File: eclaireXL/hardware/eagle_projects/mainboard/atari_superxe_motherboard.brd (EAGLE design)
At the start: 140.6 x 100.1 mm, 121 parts

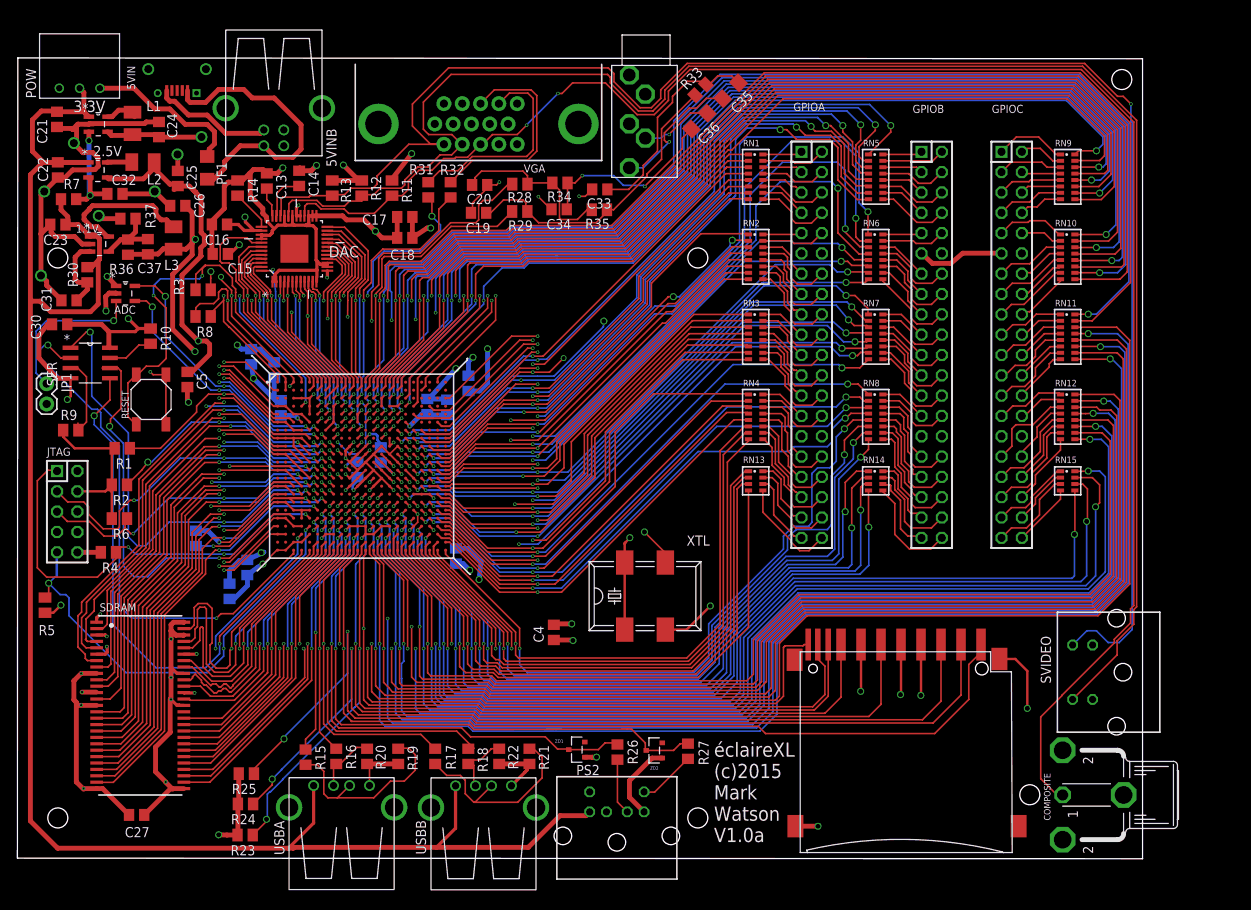
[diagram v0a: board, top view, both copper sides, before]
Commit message: Fixed audio connector footprint/location. Fixed oscilator footprint (fitted but was too large). Added 16 pin support for serial init rom. Moved reset switch location to allow this. Added pull ups and decoupling to ADC (still untested). Added some more 2.5mm drill holes on the right for stencil positioning. Increased 2.5mm drill size by 1 notch (was too small to fit). Added solder pads for din connectors. Fixed footprint for phono connector. Increased resistor array size to allow fixing by hand more easily. Added pin headers to allow bypassing resistor arrays in case of issues soldering thsm! Added pin header borders to board to make it clear how much space is needed around them for sockets. Made room for jtag pin header socket. Increased version to v1.1. Added decoupling cap to oscillator. Added voltage test point header. Power ADC by 5V (it allows 2.7V to 5.5v but higher reduces changes of breaking it by high voltage inputs I think). Think thats it. Will review a bit then make the next board revision.
git-svn-id: http://www.64kib.com/atarixlfpga_svn/trunk/atari_800xl@408 d6161ac3-aae1-4d52-9b05-ea9ac36b53d3
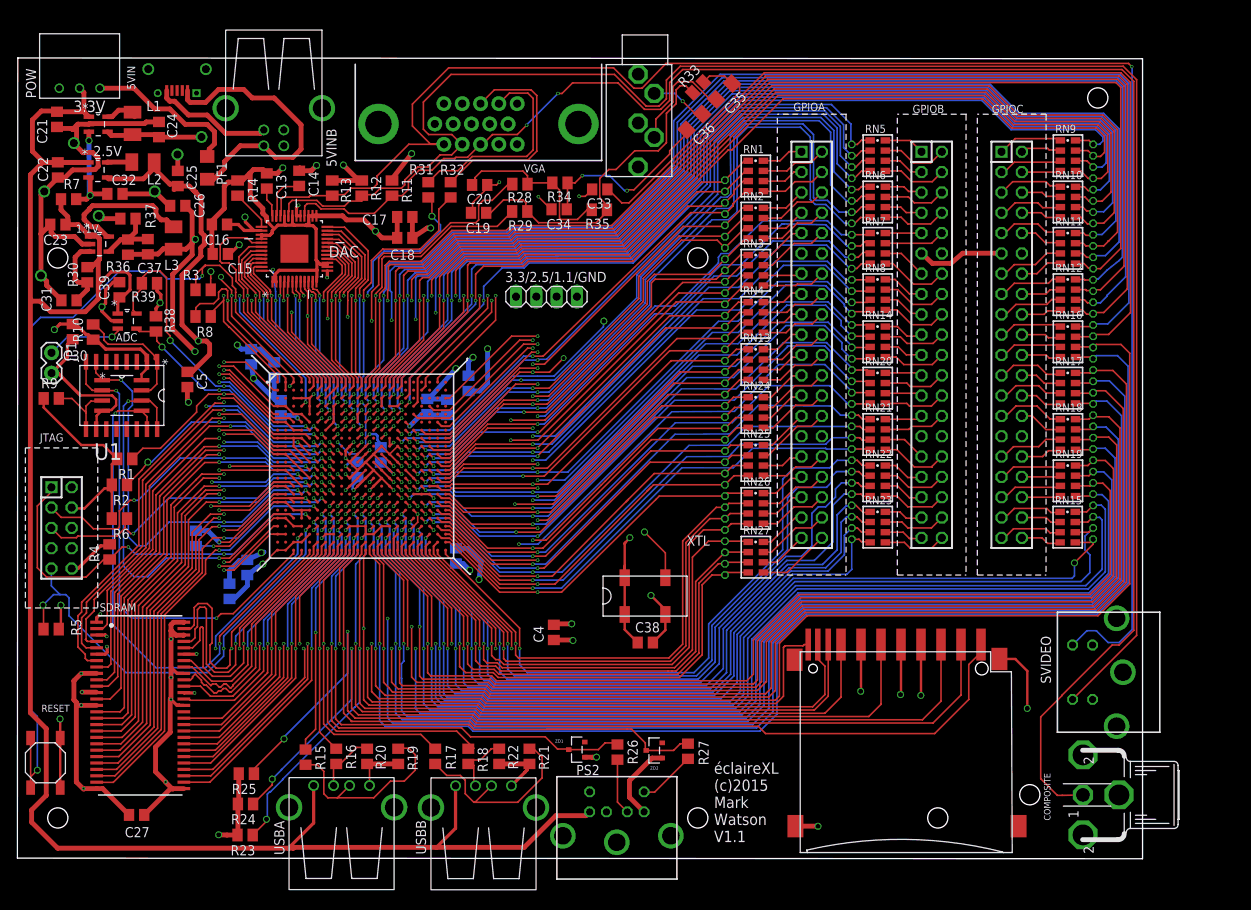
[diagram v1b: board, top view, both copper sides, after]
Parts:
- removed SER: AT25320B-SSHL-B, Atmel_By_element14_Batch_1-00:SOIC127P600X175-8N
- added 3.3/2.5/1.1/GND: (no value), pinhead:1X04
- added C38, C39: 0.1uF, rcl:C0805
- added R38, R39: 2k, rcl:M0805
- added RN16, RN17, RN18, RN19, RN20, RN21, RN22, RN23, RN24, RN25, RN26, RN27: 47, resistor-array:743-8
- added U$3, U$4, U$5: HDR_SMALL_36_DEV_LALIGNED, header127:HDR_141_36
- added U1: EPCS, epcs:EPCS_BOTH
- COMPOSITE: value TOBU3 -> TOBU3MINE; device con-hirschmann:TOBU3 -> con-hirschmann:TOBU3_EXT
- JTAG: value M-2X05-DIL-100 -> M-2X05-BORDER; device con-headers-jp:DIL-100-2X05 -> con-headers-jp:DIL-100-2X05-BRD
- RN1, RN10, RN11, RN12, RN2, RN3, RN4, RN5, RN6, RN7, RN8, RN9: device resistor-array:742-16 -> resistor-array:743-8
- RN13, RN14, RN15: device resistor-array:742-8 -> resistor-array:743-8
- XTL: device crystal:1100S -> crystal:SG-636
- moved RESET 47.3 mm to (3.45, 11.9)
- moved RN14 17.4 mm to (107.5, 64.5)
- moved RN8 15.3 mm to (107.5, 70.4)
- moved RN12 15.3 mm to (131.3, 70.4)
- moved RN13 14.5 mm to (92.3, 61.7)
- moved RN4 12.4 mm to (92.3, 67.6)
- moved RN7 11.1 mm to (107.5, 76.2)
- moved RN11 11.1 mm to (131.3, 76.2)
- moved RN3 8.32 mm to (92.3, 73.5)
- moved R10 7.19 mm to (9.42, 65.7), turned to 90 degrees
- moved RN6 6.86 mm to (107.5, 82.0)
- moved RN10 6.85 mm to (131.3, 82.0)
- moved RN15 5.79 mm to (131.2, 41.3)
- moved R9 4.65 mm to (4.18, 57.4)
- moved RN2 4.21 mm to (92.3, 79.3)
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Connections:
- net 1V1: now also 3.3/2.5/1.1/GND.3
- net 2V5: now also 3.3/2.5/1.1/GND.2
- net 3V3: now also 3.3/2.5/1.1/GND.1, C38.1, R38.2, R39.1, U1.8, U1.L$2, XTL.P$1, XTL.P$4; no longer ADC.1, SER.8, XTL.1, XTL.4
- net 5V0: now also ADC.1, C39.1
- net GND: now also 3.3/2.5/1.1/GND.4, C38.2, C39.2, U1.4, U1.L$10, XTL.P$2; no longer SER.4, XTL.2
- net GPIOA0: now also U$5.P$1
- net GPIOA1: now also U$5.P$2
- net GPIOA10: now also RN3.3, U$5.P$11; no longer RN2.3
- net GPIOA11: now also RN3.4, U$5.P$12; no longer RN2.4
- net GPIOA12: now also RN4.1, U$5.P$13; no longer RN2.5
- net GPIOA13: now also RN4.2, U$5.P$14; no longer RN2.6
- net GPIOA14: now also RN4.3, U$5.P$15; no longer RN2.7
- net GPIOA15: now also RN4.4, U$5.P$16; no longer RN2.8
- net GPIOA16: now also RN13.1, U$5.P$17; no longer RN3.1
- net GPIOA17: now also RN13.2, U$5.P$18; no longer RN3.2
- net GPIOA18: now also RN13.3, U$5.P$19; no longer RN3.3
- net GPIOA19: now also RN13.4, U$5.P$20; no longer RN3.4
- net GPIOA2: now also U$5.P$3
- net GPIOA20: now also RN24.1, U$5.P$21; no longer RN3.5
- net GPIOA21: now also RN24.2, U$5.P$22; no longer RN3.6
- net GPIOA22: now also RN24.3, U$5.P$23; no longer RN3.7
- net GPIOA23: now also RN24.4, U$5.P$24; no longer RN3.8
- net GPIOA24: now also RN25.1, U$5.P$25; no longer RN4.1
- net GPIOA25: now also RN25.2, U$5.P$26; no longer RN4.2
- net GPIOA26: now also RN25.3, U$5.P$27; no longer RN4.3
- net GPIOA27: now also RN25.4, U$5.P$28; no longer RN4.4
- net GPIOA28: now also RN26.1, U$5.P$29; no longer RN4.5
- net GPIOA29: now also RN26.2, U$5.P$30; no longer RN4.6
- net GPIOA3: now also U$5.P$4
- net GPIOA30: now also RN26.3, U$5.P$31; no longer RN4.7
- net GPIOA31: now also RN26.4, U$5.P$32; no longer RN4.8
- net GPIOA32: now also RN27.1, U$5.P$33; no longer RN13.1
- net GPIOA33: now also RN27.2, U$5.P$34; no longer RN13.2
- net GPIOA34: now also RN27.3, U$5.P$35; no longer RN13.3
- net GPIOA35: now also RN27.4, U$5.P$36; no longer RN13.4
- net GPIOA4: now also RN2.1, U$5.P$5; no longer RN1.5
- net GPIOA5: now also RN2.2, U$5.P$6; no longer RN1.6
- net GPIOA6: now also RN2.3, U$5.P$7; no longer RN1.7
- net GPIOA7: now also RN2.4, U$5.P$8; no longer RN1.8
- net GPIOA8: now also RN3.1, U$5.P$9; no longer RN2.1
- net GPIOA9: now also RN3.2, U$5.P$10; no longer RN2.2
- net GPIOB0: now also U$4.P$1
- net GPIOB1: now also U$4.P$2
- net GPIOB10: now also RN7.3, U$4.P$11; no longer RN6.3
- net GPIOB11: now also RN7.4, U$4.P$12; no longer RN6.4
- net GPIOB12: now also RN8.1, U$4.P$13; no longer RN6.5
- net GPIOB13: now also RN8.2, U$4.P$14; no longer RN6.6
- net GPIOB14: now also RN8.3, U$4.P$15; no longer RN6.7
- net GPIOB15: now also RN8.4, U$4.P$16; no longer RN6.8
- net GPIOB16: now also RN14.1, U$4.P$17; no longer RN7.1
- net GPIOB17: now also RN14.2, U$4.P$18; no longer RN7.2
- net GPIOB18: now also RN14.3, U$4.P$19; no longer RN7.3
- net GPIOB19: now also RN14.4, U$4.P$20; no longer RN7.4
- net GPIOB2: now also U$4.P$3
- net GPIOB20: now also RN20.1, U$4.P$21; no longer RN7.5
- net GPIOB21: now also RN20.2, U$4.P$22; no longer RN7.6
- net GPIOB22: now also RN20.3, U$4.P$23; no longer RN7.7
- net GPIOB23: now also RN20.4, U$4.P$24; no longer RN7.8
- net GPIOB24: now also RN21.1, U$4.P$25; no longer RN8.1
- net GPIOB25: now also RN21.2, U$4.P$26; no longer RN8.2
- net GPIOB26: now also RN21.3, U$4.P$27; no longer RN8.3
- net GPIOB27: now also RN21.4, U$4.P$28; no longer RN8.4
- net GPIOB28: now also RN22.1, U$4.P$29; no longer RN8.5
- net GPIOB29: now also RN22.2, U$4.P$30; no longer RN8.6
- net GPIOB3: now also U$4.P$4
- net GPIOB30: now also RN22.3, U$4.P$31; no longer RN8.7
- net GPIOB31: now also RN22.4, U$4.P$32; no longer RN8.8
- net GPIOB32: now also RN23.1, U$4.P$33; no longer RN14.1
- net GPIOB33: now also RN23.2, U$4.P$34; no longer RN14.2
- net GPIOB34: now also RN23.3, U$4.P$35; no longer RN14.3
- net GPIOB35: now also RN23.4, U$4.P$36; no longer RN14.4
- net GPIOB4: now also RN6.1, U$4.P$5; no longer RN5.5
- net GPIOB5: now also RN6.2, U$4.P$6; no longer RN5.6
- net GPIOB6: now also RN6.3, U$4.P$7; no longer RN5.7
- net GPIOB7: now also RN6.4, U$4.P$8; no longer RN5.8
- net GPIOB8: now also RN7.1, U$4.P$9; no longer RN6.1
- net GPIOB9: now also RN7.2, U$4.P$10; no longer RN6.2
- net GPIOC0: now also RN9.8, U$3.P$1; no longer RN9.16
- net GPIOC1: now also RN9.7, U$3.P$2; no longer RN9.15
- net GPIOC10: now also RN11.6, U$3.P$11; no longer RN10.14
- net GPIOC11: now also RN11.5, U$3.P$12; no longer RN10.13
- net GPIOC12: now also RN12.8, U$3.P$13; no longer RN10.12
- net GPIOC13: now also RN12.7, U$3.P$14; no longer RN10.11
- net GPIOC14: now also RN12.6, U$3.P$15; no longer RN10.10
- net GPIOC15: now also RN12.5, U$3.P$16; no longer RN10.9
- net GPIOC16: now also RN16.8, U$3.P$17; no longer RN11.16
- net GPIOC17: now also RN16.7, U$3.P$18; no longer RN11.15
- net GPIOC18: now also RN16.6, U$3.P$19; no longer RN11.14
- net GPIOC19: now also RN16.5, U$3.P$20; no longer RN11.13
- net GPIOC2: now also RN9.6, U$3.P$3; no longer RN9.14
- net GPIOC20: now also RN17.8, U$3.P$21; no longer RN11.12
- net GPIOC21: now also RN17.7, U$3.P$22; no longer RN11.11
- net GPIOC22: now also RN17.6, U$3.P$23; no longer RN11.10
- net GPIOC23: now also RN17.5, U$3.P$24; no longer RN11.9
- net GPIOC24: now also RN18.8, U$3.P$25; no longer RN12.16
- net GPIOC25: now also RN18.7, U$3.P$26; no longer RN12.15
- net GPIOC26: now also RN18.6, U$3.P$27; no longer RN12.14
- net GPIOC27: now also RN18.5, U$3.P$28; no longer RN12.13
- net GPIOC28: now also RN19.8, U$3.P$29; no longer RN12.12
- net GPIOC29: now also RN19.7, U$3.P$30; no longer RN12.11
- net GPIOC3: now also RN9.5, U$3.P$4; no longer RN9.13
- net GPIOC30: now also RN19.6, U$3.P$31; no longer RN12.10
- net GPIOC31: now also RN19.5, U$3.P$32; no longer RN12.9
- net GPIOC32: now also U$3.P$33
- net GPIOC33: now also U$3.P$34
- net GPIOC34: now also U$3.P$35
- net GPIOC35: now also U$3.P$36
- net GPIOC4: now also RN10.8, U$3.P$5; no longer RN9.12
- net GPIOC5: now also RN10.7, U$3.P$6; no longer RN9.11
- net GPIOC6: now also RN10.6, U$3.P$7; no longer RN9.10
- net GPIOC7: now also RN10.5, U$3.P$8; no longer RN9.9
- net GPIOC8: now also RN11.8, U$3.P$9; no longer RN10.16
- net GPIOC9: now also RN11.7, U$3.P$10; no longer RN10.15
- net N$10: now also U1.3, U1.L$9; no longer SER.3
- net N$103: now also RN10.1; no longer RN9.5
- net N$104: now also RN10.2; no longer RN9.6
- net N$105: now also RN10.3; no longer RN9.7
- net N$106: now also RN10.4; no longer RN9.8
- net N$107: now also RN11.1; no longer RN10.1
- net N$108: now also RN11.2; no longer RN10.2
- net N$109: now also RN11.3; no longer RN10.3
- net N$11: now also U1.7, U1.L$1; no longer SER.7
- net N$110: now also RN11.4; no longer RN10.4
- net N$111: now also RN12.1; no longer RN10.5
- net N$112: now also RN12.2; no longer RN10.6
- net N$113: now also RN12.3; no longer RN10.7
- net N$114: now also RN12.4; no longer RN10.8
- net N$115: now also RN16.1; no longer RN11.1
- net N$116: now also RN16.2; no longer RN11.2
- net N$117: now also RN16.3; no longer RN11.3
- net N$118: now also RN16.4; no longer RN11.4
- net N$119: now also RN17.1; no longer RN11.5
- net N$12: now also XTL.P$3; no longer XTL.3
- net N$120: now also RN17.2; no longer RN11.6
- net N$121: now also RN17.3; no longer RN11.7
- net N$122: now also RN17.4; no longer RN11.8
- net N$123: now also RN18.1; no longer RN12.1
- net N$124: now also RN18.2; no longer RN12.2
- net N$125: now also RN18.3; no longer RN12.3
- net N$126: now also RN18.4; no longer RN12.4
- net N$127: now also RN19.1; no longer RN12.5
- net N$128: now also RN19.2; no longer RN12.6
- net N$129: now also RN19.3; no longer RN12.7
- net N$130: now also RN19.4; no longer RN12.8
- net N$138: now also AUDIO.P$3; no longer AUDIO.P$5
- net N$141: now also AUDIO.P$2; no longer AUDIO.P$4
- net N$22: now also RN1.8; no longer RN1.16
- net N$24: now also RN1.7; no longer RN1.15
- net N$29: now also RN1.6; no longer RN1.14
- net N$30: now also RN1.5; no longer RN1.13
- net N$31: now also RN2.8; no longer RN1.12
- net N$32: now also RN2.7; no longer RN1.11
- net N$33: now also RN2.6; no longer RN1.10
- net N$34: now also RN2.5; no longer RN1.9
- net N$35: now also RN3.8; no longer RN2.16
- net N$36: now also RN3.7; no longer RN2.15
- net N$37: now also RN3.6; no longer RN2.14
- net N$38: now also RN3.5; no longer RN2.13
- net N$39: now also RN4.8; no longer RN2.12
- net N$40: now also RN4.6; no longer RN2.10
- net N$41: now also RN4.7; no longer RN2.11
- net N$42: now also RN4.5; no longer RN2.9
- net N$43: now also RN13.8; no longer RN3.16
- net N$44: now also RN13.7; no longer RN3.15
- net N$45: now also RN13.6; no longer RN3.14
- net N$46: now also RN13.5; no longer RN3.13
- net N$47: now also RN24.8; no longer RN3.12
- net N$48: now also RN24.6; no longer RN3.10
- net N$49: now also RN24.7; no longer RN3.11
- net N$50: now also RN24.5; no longer RN3.9
- net N$51: now also RN25.8; no longer RN4.16
- net N$52: now also RN25.7; no longer RN4.15
- net N$53: now also RN25.6; no longer RN4.14
- net N$54: now also RN25.5; no longer RN4.13
- net N$55: now also RN26.8; no longer RN4.12
- net N$56: now also RN26.7; no longer RN4.11
- net N$57: now also RN26.6; no longer RN4.10
- net N$58: now also RN26.5; no longer RN4.9
- net N$59: now also RN27.8; no longer RN13.8
- net N$6: now also U1.6, U1.L$16; no longer SER.6
- net N$60: now also RN27.7; no longer RN13.7
- net N$61: now also RN27.6; no longer RN13.6
- net N$62: now also RN27.5; no longer RN13.5
- net N$63: now also RN5.8; no longer RN5.16
- net N$64: now also RN5.7; no longer RN5.15
- net N$65: now also RN5.6; no longer RN5.14
- net N$66: now also RN5.5; no longer RN5.13
- net N$67: now also RN6.8; no longer RN5.12
- net N$68: now also RN6.7; no longer RN5.11
- net N$69: now also RN6.6; no longer RN5.10
- net N$7: now also U1.1, U1.L$7; no longer SER.1
- net N$70: now also RN6.5; no longer RN5.9
- net N$71: now also RN7.8; no longer RN6.16
- net N$72: now also RN7.7; no longer RN6.15
- net N$73: now also RN7.6; no longer RN6.14
- net N$74: now also RN7.5; no longer RN6.13
- net N$75: now also RN8.8; no longer RN6.12
- net N$76: now also RN8.7; no longer RN6.11
- net N$77: now also RN8.6; no longer RN6.10
- net N$78: now also RN8.5; no longer RN6.9
- net N$79: now also RN14.8; no longer RN7.16
- net N$8: now also U1.2, U1.L$8; no longer SER.2
- net N$80: now also RN14.7; no longer RN7.15
- net N$81: now also RN14.6; no longer RN7.14
- net N$82: now also RN14.5; no longer RN7.13
- net N$83: now also RN20.8; no longer RN7.12
- net N$84: now also RN20.7; no longer RN7.11
- net N$85: now also RN20.6; no longer RN7.10
- net N$86: now also RN20.5; no longer RN7.9
- net N$87: now also RN21.8; no longer RN8.16
- net N$88: now also RN21.7; no longer RN8.15
- net N$89: now also RN21.6; no longer RN8.14
- net N$9: now also U1.5, U1.L$15; no longer SER.5
- net N$90: now also RN21.5; no longer RN8.13
- net N$91: now also RN22.8; no longer RN8.12
- net N$92: now also RN22.7; no longer RN8.11
- net N$93: now also RN22.6; no longer RN8.10
- net N$94: now also RN22.5; no longer RN8.9
- net N$95: now also RN23.8; no longer RN14.8
- net N$96: now also RN23.7; no longer RN14.7
- net N$97: now also RN23.6; no longer RN14.6
- net N$98: now also RN23.5; no longer RN14.5
- net SCL: now also R39.2
- net SDA: now also R38.1
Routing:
- net CONFIG_N: track 53.8 -> 113.7 mm
- net 5V0: track 361.2 -> 409.5 mm
- net GPIOB8: track 92.4 -> 72.1 mm, vias 3 -> 2
- net GPIOB9: track 84.5 -> 66.8 mm, vias 2 -> 1
- net GPIOB10: track 85.4 -> 70.4 mm, vias 3 -> 2
- net GPIOB11: track 77.3 -> 66.2 mm, vias 2 -> 1
- net 3V3: track 479.6 -> 490.5 mm
- net AUDIO_IN: track 19.9 -> 9.73 mm
- net N$11: track 5.81 -> 15.7 mm
- net GPIOA34: track 73.5 -> 64.0 mm
- net GPIOA33: track 73.6 -> 64.3 mm
- net GPIOA30: track 73.9 -> 64.7 mm
- net GPIOA29: track 71.1 -> 61.9 mm
- net GPIOA35: track 79.1 -> 70.0 mm
- net GND: track 840.9 -> 850.0 mm, vias 92 -> 91
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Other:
- board text added: "éclaireXL (c)2015 Mark Watson V1.1"
- board text removed: "éclaireXL (c)2015 Mark Watson V1.0a"

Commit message: Moved traces away from mounting holes to remove risk of taking out traces with screws... Harder than expected!
git-svn-id: http://www.64kib.com/atarixlfpga_svn/trunk/atari_800xl@409 d6161ac3-aae1-4d52-9b05-ea9ac36b53d3
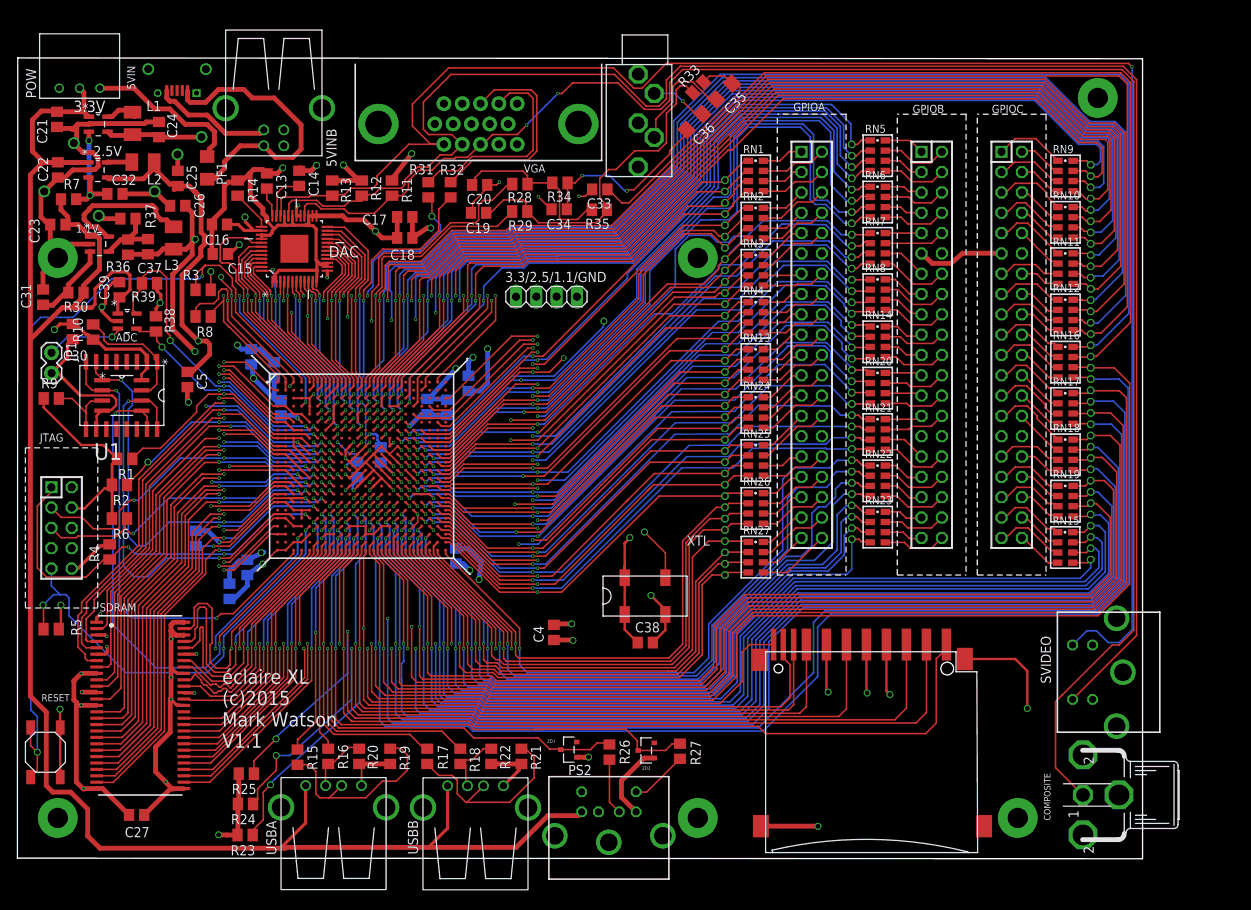
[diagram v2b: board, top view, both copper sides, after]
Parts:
- added H1, H2, H3, H4, H5, H6: MOUNT-PAD-ROUND2.5, holes:2,5-PAD
- moved U$2 4.32 mm to (106.7, 25.8)
- moved C31 3.28 mm to (3.15, 70.1), turned to 90 degrees
- moved R30 2.65 mm to (7.26, 70.7), turned to 180 degrees
- moved RN10 2.56 mm to (131.0, 79.5)
- moved RN11 2.56 mm to (131.0, 73.7)
- moved RN12 2.56 mm to (131.0, 67.9)
- moved RN16 2.56 mm to (131.0, 62.0)
- moved RN15 2.56 mm to (130.9, 38.8)
- moved RN17 2.56 mm to (131.0, 56.2)
- moved RN18 2.56 mm to (131.0, 50.4)
- moved RN19 2.56 mm to (131.0, 44.6)
- moved U$3 2.56 mm to (134.1, 61.3)
- moved RN9 2.56 mm to (131.0, 85.2)
- moved RESET 1.32 mm to (3.45, 13.2)
- moved PS2 1.00 mm to (73.9, -2.74)
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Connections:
- net GND: now also H1.B2,8, H2.B2,8, H3.B2,8, H4.B2,8, H5.B2,8, H6.B2,8
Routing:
- net GPIOB8: track 72.1 -> 78.2 mm
- net SD_WRITEPROTECT: track 85.0 -> 79.3 mm
- net GND: track 850.0 -> 855.5 mm, vias 91 -> 90
- net GPIOC19: track 164.5 -> 160.2 mm
- net SD_DETECT: track 90.0 -> 85.9 mm
- net SD_SCK: track 99.6 -> 95.7 mm
- net GPIOC18: track 162.6 -> 158.7 mm
- net SD_MOSI: track 135.0 -> 131.1 mm
- net SD_DAT1: track 84.6 -> 80.9 mm
- net CONFIG_N: track 113.7 -> 110.2 mm
- net SD_MISO: track 117.5 -> 114.1 mm
- net N$143: track 217.2 -> 213.8 mm
- net GPIOC21: track 164.3 -> 160.9 mm
- net 3V3: track 490.5 -> 493.4 mm
- net GPIOC25: track 148.5 -> 145.7 mm
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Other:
- board text added: "éclaire XL (c)2015 Mark Watson V1.1"
- board text removed: "éclaireXL (c)2015 Mark Watson V1.1"

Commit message: DE1 connector spacing (20mm). Improved mounting holes.
git-svn-id: http://www.64kib.com/atarixlfpga_svn/trunk/atari_800xl@411 d6161ac3-aae1-4d52-9b05-ea9ac36b53d3
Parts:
- moved H6 20.0 mm to (145.0, 5.00)
- moved GPIOC 15.0 mm to (139.2, 64.1)
- moved R25 10.3 mm to (20.0, 4.79), turned to 270 degrees
- moved H1 10.0 mm to (145.0, 95.0)
- moved SVIDEO 9.79 mm to (152.1, 20.1)
- moved U$3 5.51 mm to (129.0, 59.2)
- moved R24 5.07 mm to (23.8, 4.69), turned to 270 degrees
- moved GPIOB 5.00 mm to (119.2, 64.1)
- moved RN14 5.00 mm to (112.5, 64.5)
- moved RN20 5.00 mm to (112.5, 58.7)
- moved RN21 5.00 mm to (112.5, 52.9)
- moved RN22 5.00 mm to (112.5, 47.1)
- moved RN23 5.00 mm to (112.5, 41.4)
- moved RN5 5.00 mm to (112.5, 87.8)
- moved RN6 5.00 mm to (112.5, 82.0)
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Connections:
- removed net N$134: GPIOC.40, RN15.4
- new net N$15: GPIOC.1, RN9.8
- net GPIOC0: now also RN9.1, U$1.B12; no longer RN9.8, U$1.C15
- net GPIOC1: now also RN9.2, U$1.D12; no longer RN9.7, U$1.E15
- net GPIOC10: now also RN11.3, U$1.A14; no longer RN11.6, U$1.C13
- net GPIOC11: now also RN11.4, U$1.E14; no longer RN11.5, U$1.D13
- net GPIOC12: now also RN12.1, U$1.F14; no longer RN12.8, U$1.B13
- net GPIOC13: now also RN12.2, U$1.H14; no longer RN12.7, U$1.A13
- net GPIOC14: now also RN12.3, U$1.A15; no longer RN12.6, U$1.F12
- net GPIOC15: now also RN12.4, U$1.B15; no longer RN12.5, U$1.E12
- net GPIOC16: now also RN16.1, U$1.E15; no longer RN16.8, U$1.D12
- net GPIOC17: now also RN16.2, U$1.C15; no longer RN16.7, U$1.B12
- net GPIOC18: now also RN16.3, U$1.Y16; no longer RN16.6, U$1.V13
- net GPIOC19: now also RN16.4, U$1.V16; no longer RN16.5, U$1.AA13
- net GPIOC2: now also RN9.3, U$1.E12; no longer RN9.6, U$1.B15
- net GPIOC20: now also RN17.1, U$1.W16; no longer RN17.8, U$1.AB13
- net GPIOC21: now also RN17.2, U$1.U16; no longer RN17.7, U$1.R14
- net GPIOC22: now also RN17.3, U$1.AB15; no longer RN17.6, U$1.T14
- net GPIOC23: now also RN17.4, U$1.AA15; no longer RN17.5, U$1.Y14
- net GPIOC24: now also RN18.1, U$1.V15; no longer RN18.8, U$1.V14
- net GPIOC25: now also RN18.2, U$1.Y15; no longer RN18.7, U$1.AA14
- net GPIOC26: now also RN18.3, U$1.U15; no longer RN18.6, U$1.T15
- net GPIOC27: now also RN18.4, U$1.T15; no longer RN18.5, U$1.U15
- net GPIOC28: now also RN19.1, U$1.AA14; no longer RN19.8, U$1.Y15
- net GPIOC29: now also RN19.2, U$1.V14; no longer RN19.7, U$1.V15
- net GPIOC3: now also RN9.4, U$1.F12; no longer RN9.5, U$1.A15
- net GPIOC30: now also RN19.3, U$1.Y14; no longer RN19.6, U$1.AA15
- net GPIOC31: now also RN19.4, U$1.T14; no longer RN19.5, U$1.AB15
- net GPIOC32: now also RN15.1, U$1.R14; no longer RN15.8, U$1.U16
- net GPIOC33: now also RN15.2, U$1.AB13; no longer RN15.7, U$1.W16
- net GPIOC34: now also RN15.3, U$1.AA13; no longer RN15.6, U$1.V16
- net GPIOC35: now also RN15.4, U$1.V13; no longer RN15.5, U$1.Y16
- net GPIOC4: now also RN10.1, U$1.A13; no longer RN10.8, U$1.H14
- net GPIOC5: now also RN10.2, U$1.B13; no longer RN10.7, U$1.F14
- net GPIOC6: now also RN10.3, U$1.D13; no longer RN10.6, U$1.E14
- net GPIOC7: now also RN10.4, U$1.C13; no longer RN10.5, U$1.A14
- net GPIOC8: now also RN11.1, U$1.F13; no longer RN11.8, U$1.G13
- net GPIOC9: now also RN11.2, U$1.G13; no longer RN11.7, U$1.F13
- net N$100: now also GPIOC.3, RN9.6; no longer GPIOC.2, RN9.2
- net N$101: now also GPIOC.4, RN9.5; no longer GPIOC.3, RN9.3
- net N$102: now also GPIOC.5, RN10.8; no longer GPIOC.4, RN9.4
- net N$103: now also GPIOC.6, RN10.7; no longer GPIOC.5, RN10.1
- net N$104: now also GPIOC.7, RN10.6; no longer GPIOC.6, RN10.2
- net N$105: now also GPIOC.8, RN10.5; no longer GPIOC.7, RN10.3
- net N$106: now also GPIOC.9, RN11.8; no longer GPIOC.8, RN10.4
- net N$107: now also GPIOC.10, RN11.7; no longer GPIOC.9, RN11.1
- net N$108: now also GPIOC.13, RN11.6; no longer GPIOC.10, RN11.2
- net N$109: now also GPIOC.14, RN11.5; no longer GPIOC.13, RN11.3
- net N$110: now also GPIOC.15, RN12.8; no longer GPIOC.14, RN11.4
- net N$111: now also GPIOC.16, RN12.7; no longer GPIOC.15, RN12.1
- net N$112: now also GPIOC.17, RN12.6; no longer GPIOC.16, RN12.2
- net N$113: now also GPIOC.18, RN12.5; no longer GPIOC.17, RN12.3
- net N$114: now also GPIOC.19, RN16.8; no longer GPIOC.18, RN12.4
- net N$115: now also GPIOC.20, RN16.7; no longer GPIOC.19, RN16.1
- net N$116: now also GPIOC.21, RN16.6; no longer GPIOC.20, RN16.2
- net N$117: now also GPIOC.22, RN16.5; no longer GPIOC.21, RN16.3
- net N$118: now also GPIOC.23, RN17.8; no longer GPIOC.22, RN16.4
- net N$119: now also GPIOC.24, RN17.7; no longer GPIOC.23, RN17.1
- net N$120: now also GPIOC.25, RN17.6; no longer GPIOC.24, RN17.2
- net N$121: now also GPIOC.26, RN17.5; no longer GPIOC.25, RN17.3
- net N$122: now also GPIOC.27, RN18.8; no longer GPIOC.26, RN17.4
- net N$123: now also GPIOC.28, RN18.7; no longer GPIOC.27, RN18.1
- net N$124: now also GPIOC.31, RN18.6; no longer GPIOC.28, RN18.2
- net N$125: now also GPIOC.32, RN18.5; no longer GPIOC.31, RN18.3
- net N$126: now also GPIOC.33, RN19.8; no longer GPIOC.32, RN18.4
- net N$127: now also GPIOC.34, RN19.7; no longer GPIOC.33, RN19.1
- net N$128: now also GPIOC.35, RN19.6; no longer GPIOC.34, RN19.2
- net N$129: now also GPIOC.36, RN19.5; no longer GPIOC.35, RN19.3
- net N$130: now also GPIOC.37, RN15.8; no longer GPIOC.36, RN19.4
- net N$131: now also GPIOC.38, RN15.7; no longer GPIOC.37, RN15.1
- net N$132: now also GPIOC.39, RN15.6; no longer GPIOC.38, RN15.2
- net N$133: now also GPIOC.40, RN15.5; no longer GPIOC.39, RN15.3
- net N$99: now also GPIOC.2, RN9.7; no longer GPIOC.1, RN9.1
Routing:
- net GPIOC21: track 160.9 -> 130.1 mm
- net GPIOC18: track 158.7 -> 128.7 mm, vias 2 -> 1
- net GPIOC19: track 160.2 -> 130.4 mm, vias 1 -> 2
- net GPIOC16: track 163.0 -> 133.7 mm
- net GPIOC14: track 157.4 -> 129.4 mm, vias 2 -> 1
- net GPIOC23: track 152.0 -> 125.0 mm, vias 2 -> 1
- net GPIOC22: track 150.8 -> 124.6 mm, vias 2 -> 1
- net GPIOC25: track 145.7 -> 121.3 mm, vias 1 -> 2
- net GPIOC15: track 159.0 -> 136.6 mm, vias 2 -> 1
- net 5V0: track 408.9 -> 431.0 mm
- net GPIOC20: track 150.0 -> 128.5 mm, vias 1 -> 2
- net GPIOC17: track 159.2 -> 138.7 mm, vias 1 -> 2
- net GPIOC27: track 144.1 -> 125.0 mm
- net GPIOC10: track 143.9 -> 124.9 mm, vias 2 -> 1
- net SD_CS: track 132.9 -> 151.3 mm
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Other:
- board size 140.6 x 100.1 mm -> 150 x 100 mm
